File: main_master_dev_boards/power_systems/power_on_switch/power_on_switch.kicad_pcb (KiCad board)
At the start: 2 copper layers, 30.7 x 28.2 mm, 14 parts, among them J1 Vbackup_in, J2 GND_in, J3 24_in, J4 Switch_out, J5 24_out, J6 GND_in, J7 GND_out, Q1 PSMN013-80YS, SW1 SW_Push, U1 LTC2955-1

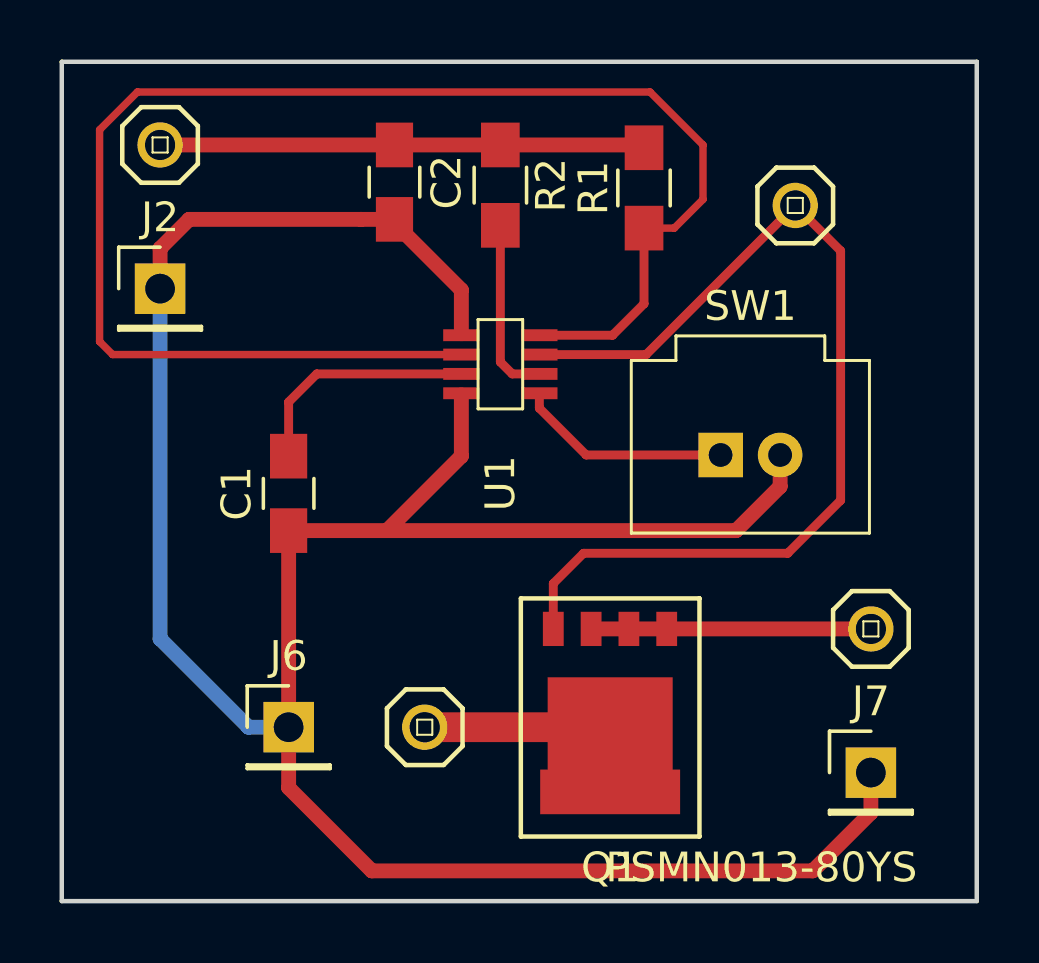
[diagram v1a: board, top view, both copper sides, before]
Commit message: Modifying power switch dev board so that tracing and pads are bigger to make soldering easier.
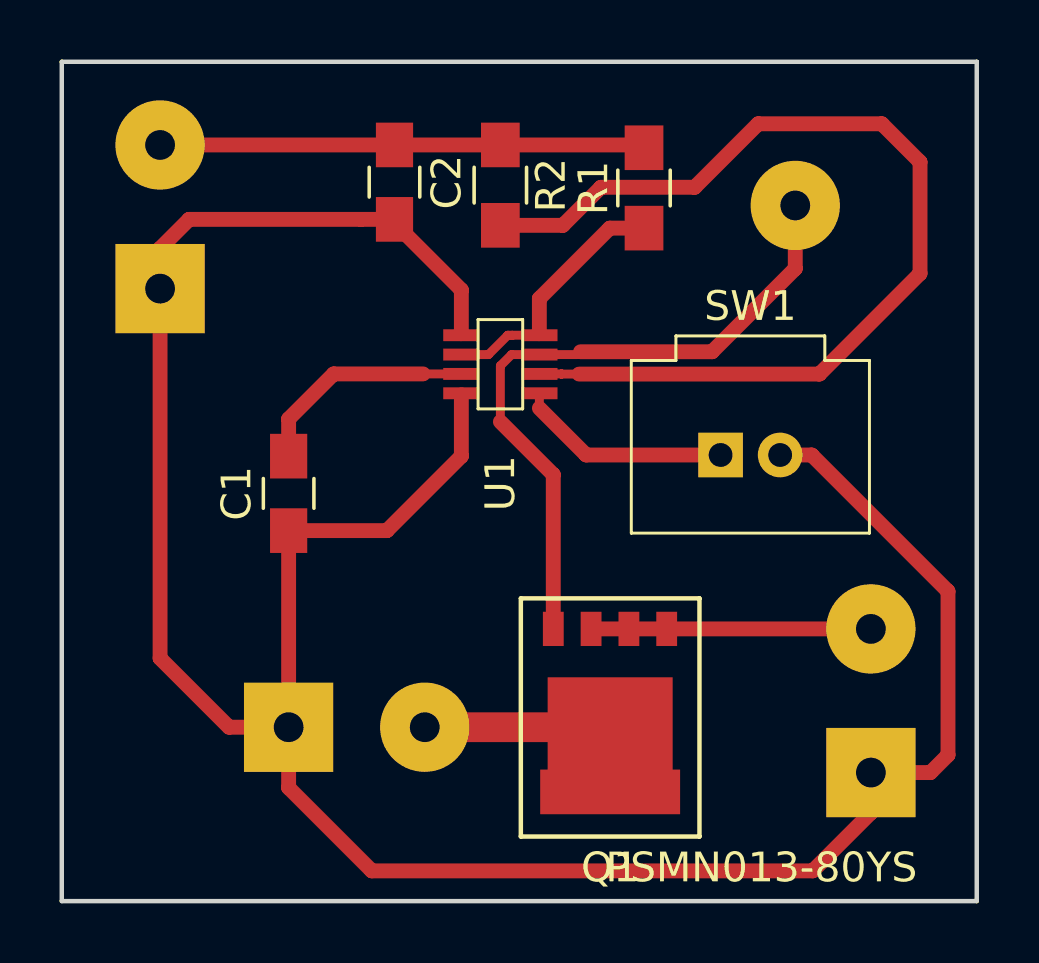
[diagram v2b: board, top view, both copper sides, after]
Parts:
- J1, J3, J4, J5: footprint pinhead:pinhead-1X01 -> pinheaders:pinhead-01x01_3x1
- J2, J6, J7: footprint Pin_Headers:Pin_Header_Straight_1x01_Pitch2.54mm -> pinheaders:pinhead-01x01_3x1_square
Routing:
- net Net-(R1-Pad1): track 51.7 -> 8.57 mm
- net Net-(R2-Pad2): track 6.07 -> 34.0 mm
- net /Switch_on: track 33.5 -> 23.0 mm
- net GND: track 87.0 -> 89.7 mm

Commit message: Redesigned 24 to 5 dev board
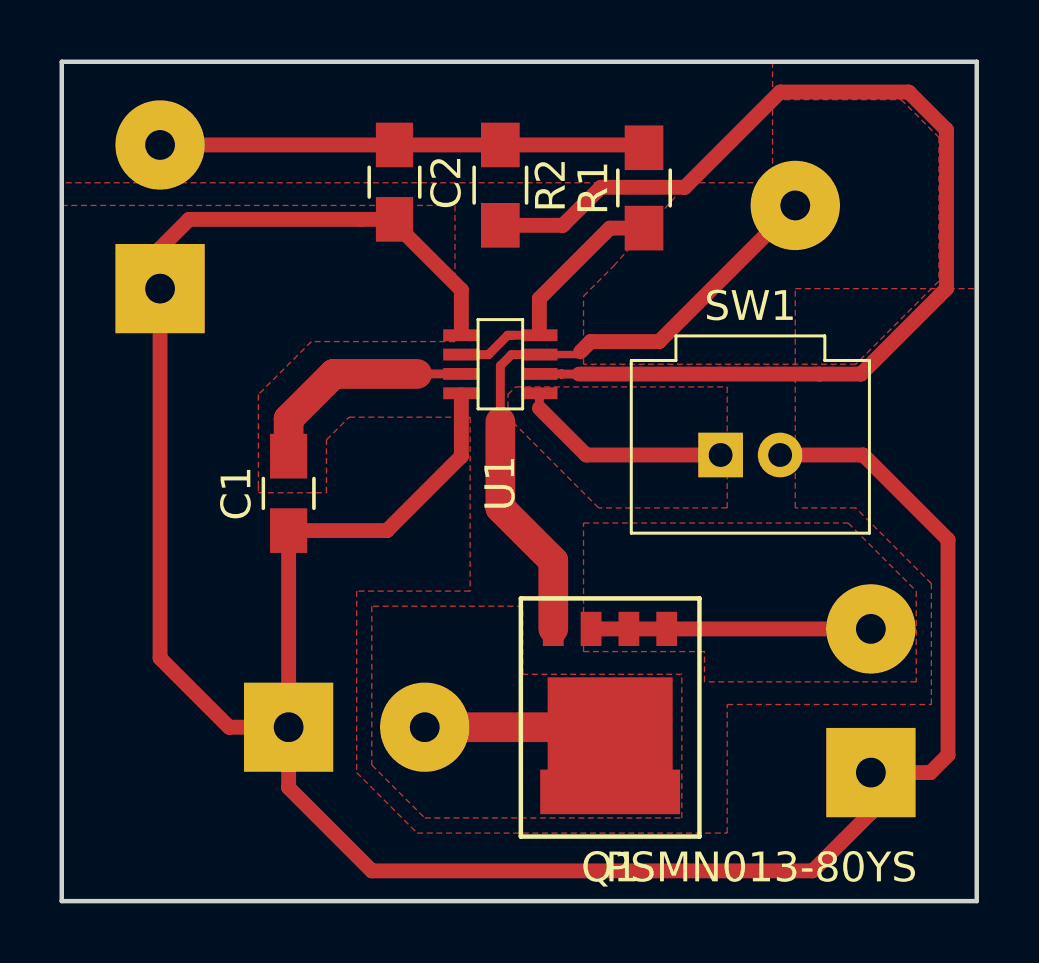
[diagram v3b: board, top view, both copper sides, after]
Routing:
- net Net-(R2-Pad2): track 34.0 -> 37.6 mm
- net /Switch_on: track 23.0 -> 21.7 mm
- net GND: track 89.7 -> 90.7 mm
- added copper zone on F.Cu, net /Switch_on
- added copper zone on F.Cu, net /V24_in
- added copper zone on F.Cu, net /V24_on
- added copper zone on F.Cu, net /Vbackup_in
- added copper zone on F.Cu, net GND
- added copper zone on F.Cu, net Net-(SW1-Pad1)
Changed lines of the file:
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@@
-(kicad_pcb (version 4) (host pcbnew 4.0.4-stable)
+(kicad_pcb (version 4) (host pcbnew 4.0.6)
   (general
     (links 22)
-    (no_connects 5)
-    (area 125.908999 53.010999 156.793001 81.355001)
+    (no_connects 0)
+    (area 125.908999 52.23275 159.882953 81.355001)
     (thickness 1.6)
     (drawings 4)
-    (tracks 71)
+    (tracks 74)
     (zones 0)
     (modules 14)
@@
   (gr_line (start 156.718 53.086) (end 156.718 81.28) (layer Edge.Cuts) (width 0.15))
   (gr_line (start 125.984 53.086) (end 156.718 53.086) (layer Edge.Cuts) (width 0.15))
-  (segment (start 155.7528 70.87214) (end 155.7528 76.3712) (width 0.5) (layer F.Cu) (net 1))
+  (segment (start 150.114 66.294) (end 152.908 66.294) (width 0.5) (layer F.Cu) (net 1))
+  (segment (start 152.908 66.294) (end 155.7528 69.1388) (width 0.5) (layer F.Cu) (net 1))
+  (segment (start 155.7528 69.1388) (end 155.7528 76.3712) (width 0.5) (layer F.Cu) (net 1))
   (segment (start 155.7528 76.3712) (end 155.162 76.962) (width 0.5) (layer F.Cu) (net 1))
   (segment (start 155.162 76.962) (end 153.162 76.962) (width 0.5) (layer F.Cu) (net 1))
-  (segment (start 150.114 66.294) (end 151.17466 66.294) (width 0.5) (layer F.Cu) (net 1))
-  (segment (start 151.17466 66.294) (end 155.7528 70.87214) (width 0.5) (layer F.Cu) (net 1))
   (segment (start 129.286 60.706) (end 129.286 73.12) (width 0.5) (layer F.Cu) (net 1))
   (segment (start 129.286 73.12) (end 131.604 75.438) (width 0.5) (layer F.Cu) (net 1))
@@
   (segment (start 130.262 58.38) (end 136.035 58.38) (width 0.5) (layer F.Cu) (net 1))
   (segment (start 136.035 58.38) (end 137.16 58.38) (width 0.5) (layer F.Cu) (net 1))
+  (segment (start 137.922 63.571) (end 138.1252 63.571) (width 0.5) (layer F.Cu) (net 2))
+  (segment (start 135.117 63.571) (end 137.922 63.571) (width 1) (layer F.Cu) (net 2))
+  (segment (start 133.604 65.084) (end 135.117 63.571) (width 1) (layer F.Cu) (net 2))
+  (segment (start 133.604 66.334) (end 133.604 65.084) (width 1) (layer F.Cu) (net 2))
   (segment (start 138.1252 63.571) (end 139.406 63.571) (width 0.3) (layer F.Cu) (net 2))
-  (segment (start 133.604 66.334) (end 133.604 65.084) (width 0.5) (layer F.Cu) (net 2))
-  (segment (start 133.604 65.084) (end 135.117 63.571) (width 0.5) (layer F.Cu) (net 2))
-  (segment (start 135.117 63.571) (end 138.1252 63.571) (width 0.5) (layer F.Cu) (net 2))
   (segment (start 140.716 55.88) (end 145.448 55.88) (width 0.5) (layer F.Cu) (net 3))
   (segment (start 145.448 55.88) (end 145.542 55.974) (width 0.5) (layer F.Cu) (net 3))
@@
   (segment (start 138.176 75.438) (end 144.277 75.438) (width 1) (layer F.Cu) (net 4))
   (segment (start 144.277 75.438) (end 144.404 75.311) (width 1) (layer F.Cu) (net 4))
-  (segment (start 140.716 65.1764) (end 142.494 66.9544) (width 0.5) (layer F.Cu) (net 5))
-  (segment (start 142.494 66.9544) (end 142.494 72.136) (width 0.5) (layer F.Cu) (net 5))
+  (segment (start 142.494 69.85) (end 140.716 68.072) (width 1) (layer F.Cu) (net 5))
+  (segment (start 140.716 68.072) (end 140.716 65.1764) (width 1) (layer F.Cu) (net 5))
+  (segment (start 142.494 72.136) (end 142.494 69.85) (width 1) (layer F.Cu) (net 5))
+  (segment (start 142.026 62.921) (end 143.31359 62.921) (width 0.25) (layer F.Cu) (net 5))
+  (segment (start 143.31359 62.921) (end 143.4084 62.82619) (width 0.25) (layer F.Cu) (net 5))
+  (segment (start 146.05 62.484) (end 143.75059 62.484) (width 0.5) (layer F.Cu) (net 5))
+  (segment (start 143.75059 62.484) (end 143.4084 62.82619) (width 0.5) (layer F.Cu) (net 5))
+  (segment (start 150.622 57.912) (end 146.05 62.484) (width 0.5) (layer F.Cu) (net 5))
   (segment (start 140.716 63.298831) (end 140.716 65.1764) (width 0.3) (layer F.Cu) (net 5))
   (segment (start 142.026 62.921) (end 141.093831 62.921) (width 0.3) (layer F.Cu) (net 5))
   (segment (start 141.093831 62.921) (end 140.716 63.298831) (width 0.3) (layer F.Cu) (net 5))
-  (segment (start 143.4084 62.82619) (end 143.31359 62.921) (width 0.3) (layer F.Cu) (net 5))
-  (segment (start 143.31359 62.921) (end 142.026 62.921) (width 0.3) (layer F.Cu) (net 5))
-  (segment (start 147.82913 62.82619) (end 143.4084 62.82619) (width 0.5) (layer F.Cu) (net 5))
-  (segment (start 150.622 57.912) (end 150.622 60.03332) (width 0.5) (layer F.Cu) (net 5))
-  (segment (start 150.622 60.03332) (end 147.82913 62.82619) (width 0.5) (layer F.Cu) (net 5))
   (segment (start 146.304 72.136) (end 153.162 72.136) (width 0.5) (layer F.Cu) (net 6))
   (segment (start 145.034 72.136) (end 146.304 72.136) (width 0.5) (layer F.Cu) (net 6))
@@
   (segment (start 140.966 62.271) (end 141.116 62.271) (width 0.3) (layer F.Cu) (net 7))
   (segment (start 141.116 62.271) (end 142.026 62.271) (width 0.3) (layer F.Cu) (net 7))
+  (segment (start 140.716 58.58) (end 142.8166 58.58) (width 0.5) (layer F.Cu) (net 8))
+  (segment (start 146.9136 57.3024) (end 150.114 54.102) (width 0.5) (layer F.Cu) (net 8))
+  (segment (start 150.114 54.102) (end 154.432 54.102) (width 0.5) (layer F.Cu) (net 8))
+  (segment (start 152.8318 63.5762) (end 151.4348 63.5762) (width 0.5) (layer F.Cu) (net 8))
+  (segment (start 142.8166 58.58) (end 144.0942 57.3024) (width 0.5) (layer F.Cu) (net 8))
+  (segment (start 144.0942 57.3024) (end 146.9136 57.3024) (width 0.5) (layer F.Cu) (net 8))
+  (segment (start 154.432 54.102) (end 155.702 55.372) (width 0.5) (layer F.Cu) (net 8))
+  (segment (start 155.702 55.372) (end 155.702 60.706) (width 0.5) (layer F.Cu) (net 8))
+  (segment (start 155.702 60.706) (end 152.8318 63.5762) (width 0.5) (layer F.Cu) (net 8))
+  (segment (start 151.4348 63.5762) (end 143.3576 63.5762) (width 0.5) (layer F.Cu) (net 8))
   (segment (start 143.3576 63.5762) (end 142.7734 63.5762) (width 0.3) (layer F.Cu) (net 8))
   (segment (start 142.7734 63.5762) (end 142.7682 63.571) (width 0.3) (layer F.Cu) (net 8))
   (segment (start 142.7682 63.571) (end 142.026 63.571) (width 0.3) (layer F.Cu) (net 8))
-  (segment (start 151.4348 63.5762) (end 143.3576 63.5762) (width 0.5) (layer F.Cu) (net 8))
-  (segment (start 154.813 60.198) (end 151.4348 63.5762) (width 0.5) (layer F.Cu) (net 8))
-  (segment (start 154.813 56.4515) (end 154.813 60.198) (width 0.5) (layer F.Cu) (net 8))
-  (segment (start 153.5303 55.1688) (end 154.813 56.4515) (width 0.5) (layer F.Cu) (net 8))
-  (segment (start 149.3774 55.1688) (end 153.5303 55.1688) (width 0.5) (layer F.Cu) (net 8))
-  (segment (start 147.2438 57.3024) (end 149.3774 55.1688) (width 0.5) (layer F.Cu) (net 8))
-  (segment (start 144.0942 57.3024) (end 147.2438 57.3024) (width 0.5) (layer F.Cu) (net 8))
-  (segment (start 142.8166 58.58) (end 144.0942 57.3024) (width 0.5) (layer F.Cu) (net 8))
-  (segment (start 140.716 58.58) (end 142.8166 58.58) (width 0.5) (layer F.Cu) (net 8))
   (segment (start 148.114 66.294) (end 143.599 66.294) (width 0.5) (layer F.Cu) (net 9))
   (segment (start 143.599 66.294) (end 142.026 64.721) (width 0.5) (layer F.Cu) (net 9))
   (segment (start 142.026 64.721) (end 142.026 64.221) (width 0.3) (layer F.Cu) (net 9))
+  (zone (net 3) (net_name /Vbackup_in) (layer F.Cu) (hatch edge 0.508)
+    (connect_pads (clearance 0.508))
+    (min_thickness 0.254)
+    (fill yes (arc_segments 16) (thermal_gap 0.508) (thermal_bridge_width 0.508))
+    (polygon
+      (pts
+        (xy 125.984 53.086) (xy 149.86 53.086) (xy 149.86 57.15) (xy 125.984 57.15)
+      )
+    )
+  )
+  (zone (net 5) (net_name /Switch_on) (layer F.Cu) (hatch edge 0.508)
+    (connect_pads (clearance 0.508))
+    (min_thickness 0.254)
+    (fill yes (arc_segments 16) (thermal_gap 0.508) (thermal_bridge_width 0.508))
+    (polygon
+      (pts
+        (xy 149.606 54.356) (xy 154.178 54.356) (xy 155.448 55.626) (xy 155.448 60.452) (xy 152.654 63.246)
+        (xy 143.51 63.246) (xy 143.51 60.96) (xy 144.526 59.944) (xy 148.59 55.372)
+      )
+    )
+  )
+  (zone (net 9) (net_name "Net-(SW1-Pad1)") (layer F.Cu) (hatch edge 0.508)
+    (connect_pads (clearance 0.508))
+    (min_thickness 0.254)
+    (fill yes (arc_segments 16) (thermal_gap 0.508) (thermal_bridge_width 0.508))
+    (polygon
+      (pts
+        (xy 141.224 64.008) (xy 148.336 64.008) (xy 148.336 68.072) (xy 144.018 68.072) (xy 140.97 65.024)
+        (xy 140.97 64.262)
+      )
+    )
+  )
+  (zone (net 6) (net_name /V24_on) (layer F.Cu) (hatch edge 0.508)
+    (connect_pads (clearance 0.508))
+    (min_thickness 0.254)
+    (fill yes (arc_segments 16) (thermal_gap 0.508) (thermal_bridge_width 0.508))
+    (polygon
+      (pts
+        (xy 143.51 72.898) (xy 143.51 68.58) (xy 151.892 68.58) (xy 152.4 68.58) (xy 154.686 70.866)
+        (xy 154.686 73.914) (xy 147.574 73.914) (xy 147.574 72.898)
+      )
+    )
+  )
+  (zone (net 1) (net_name GND) (layer F.Cu) (hatch edge 0.508)
+    (connect_pads (clearance 0.508))
+    (min_thickness 0.254)
+    (fill yes (arc_segments 16) (thermal_gap 0.508) (thermal_bridge_width 0.508))
+    (polygon
+      (pts
+        (xy 150.622 68.072) (xy 150.622 60.706) (xy 156.718 60.706) (xy 156.718 81.28) (xy 125.984 81.28)
+        (xy 125.984 57.912) (xy 139.192 57.912) (xy 139.192 62.484) (xy 134.366 62.484) (xy 132.588 64.262)
+        (xy 132.588 67.31) (xy 132.588 67.564) (xy 134.874 67.564) (xy 134.874 65.786) (xy 135.636 65.024)
+        (xy 139.7 65.024) (xy 139.7 70.866) (xy 135.89 70.866) (xy 135.89 76.962) (xy 137.922 78.994)
+        (xy 148.336 78.994) (xy 148.336 74.676) (xy 155.194 74.676) (xy 155.194 70.612) (xy 152.654 68.072)
+      )
+    )
+  )
+  (zone (net 4) (net_name /V24_in) (layer F.Cu) (hatch edge 0.508)
+    (connect_pads (clearance 0.508))
+    (min_thickness 0.254)
+    (fill yes (arc_segments 16) (thermal_gap 0.508) (thermal_bridge_width 0.508))
+    (polygon
+      (pts
+        (xy 136.398 71.374) (xy 136.398 76.708) (xy 138.176 78.486) (xy 146.812 78.486) (xy 146.812 73.66)
+        (xy 141.478 73.66) (xy 141.478 71.374)
+      )
+    )
+  )
 )

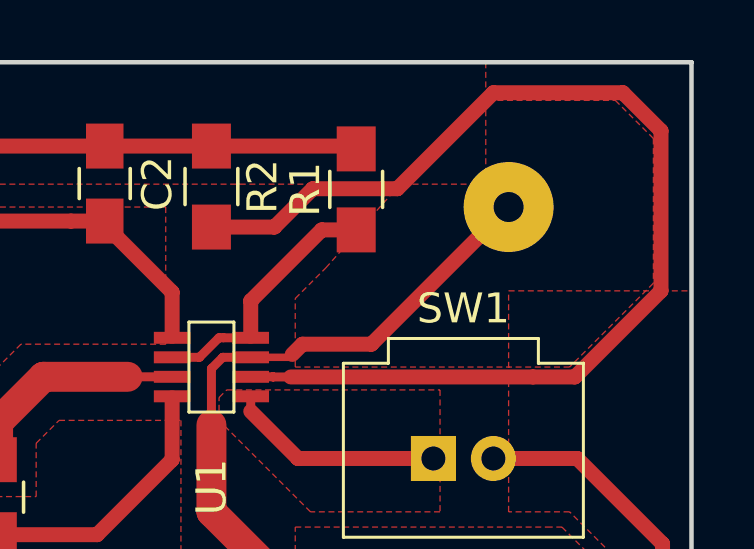
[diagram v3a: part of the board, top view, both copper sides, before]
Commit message: refined the two dev boards 24_to_5 and power_switch
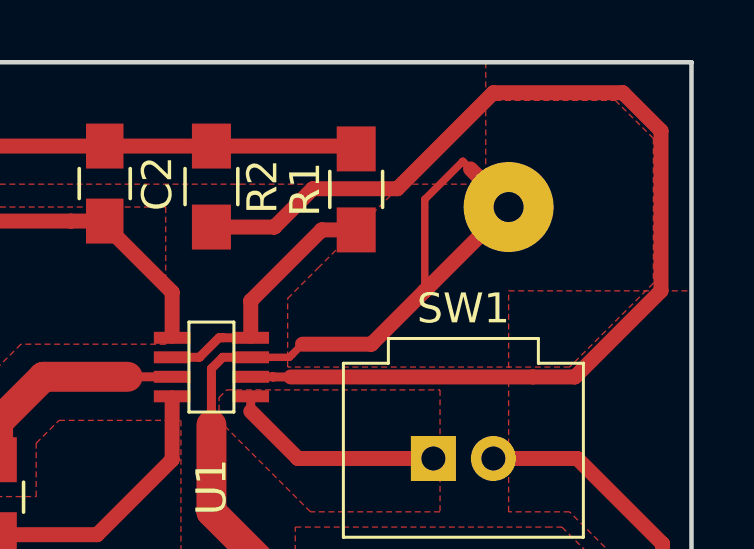
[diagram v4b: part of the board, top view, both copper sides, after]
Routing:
- net /Switch_on: track 21.7 -> 29.1 mm
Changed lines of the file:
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@@
-(kicad_pcb (version 4) (host pcbnew 4.0.6)
+(kicad_pcb (version 4) (host pcbnew 4.0.4-stable)
   (general
     (links 22)
@@
     (thickness 1.6)
     (drawings 4)
-    (tracks 74)
+    (tracks 80)
     (zones 0)
     (modules 14)
@@
   (segment (start 138.176 75.438) (end 144.277 75.438) (width 1) (layer F.Cu) (net 4))
   (segment (start 144.277 75.438) (end 144.404 75.311) (width 1) (layer F.Cu) (net 4))
+  (segment (start 150.622 57.912) (end 149.606 56.896) (width 0.5) (layer F.Cu) (net 5))
+  (segment (start 149.606 56.896) (end 149.352 56.642) (width 0.5) (layer F.Cu) (net 5))
+  (segment (start 149.098 56.388) (end 149.606 56.896) (width 0.25) (layer F.Cu) (net 5))
+  (segment (start 147.828 57.658) (end 149.098 56.388) (width 0.25) (layer F.Cu) (net 5))
+  (segment (start 147.828 60.706) (end 146.05 62.484) (width 0.5) (layer F.Cu) (net 5))
+  (segment (start 147.828 60.706) (end 147.828 57.658) (width 0.25) (layer F.Cu) (net 5))
+  (segment (start 150.622 57.912) (end 147.828 60.706) (width 0.5) (layer F.Cu) (net 5))
+  (segment (start 143.4084 62.82619) (end 143.75059 62.484) (width 0.25) (layer F.Cu) (net 5))
   (segment (start 142.494 69.85) (end 140.716 68.072) (width 1) (layer F.Cu) (net 5))
   (segment (start 140.716 68.072) (end 140.716 65.1764) (width 1) (layer F.Cu) (net 5))
@@
   (segment (start 143.31359 62.921) (end 143.4084 62.82619) (width 0.25) (layer F.Cu) (net 5))
   (segment (start 146.05 62.484) (end 143.75059 62.484) (width 0.5) (layer F.Cu) (net 5))
-  (segment (start 143.75059 62.484) (end 143.4084 62.82619) (width 0.5) (layer F.Cu) (net 5))
-  (segment (start 150.622 57.912) (end 146.05 62.484) (width 0.5) (layer F.Cu) (net 5))
   (segment (start 140.716 63.298831) (end 140.716 65.1764) (width 0.3) (layer F.Cu) (net 5))
   (segment (start 142.026 62.921) (end 141.093831 62.921) (width 0.3) (layer F.Cu) (net 5))
@@
     (polygon
       (pts
-        (xy 149.606 54.356) (xy 154.178 54.356) (xy 155.448 55.626) (xy 155.448 60.452) (xy 152.654 63.246)
-        (xy 143.51 63.246) (xy 143.51 60.96) (xy 144.526 59.944) (xy 148.59 55.372)
+        (xy 149.86 54.356) (xy 154.178 54.356) (xy 155.448 55.626) (xy 155.448 60.452) (xy 152.654 63.246)
+        (xy 143.256 63.246) (xy 143.256 60.96) (xy 144.272 59.944) (xy 148.844 55.372)
       )
     )
